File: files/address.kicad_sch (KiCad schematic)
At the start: 2 parts, among them J1 VLB_slot

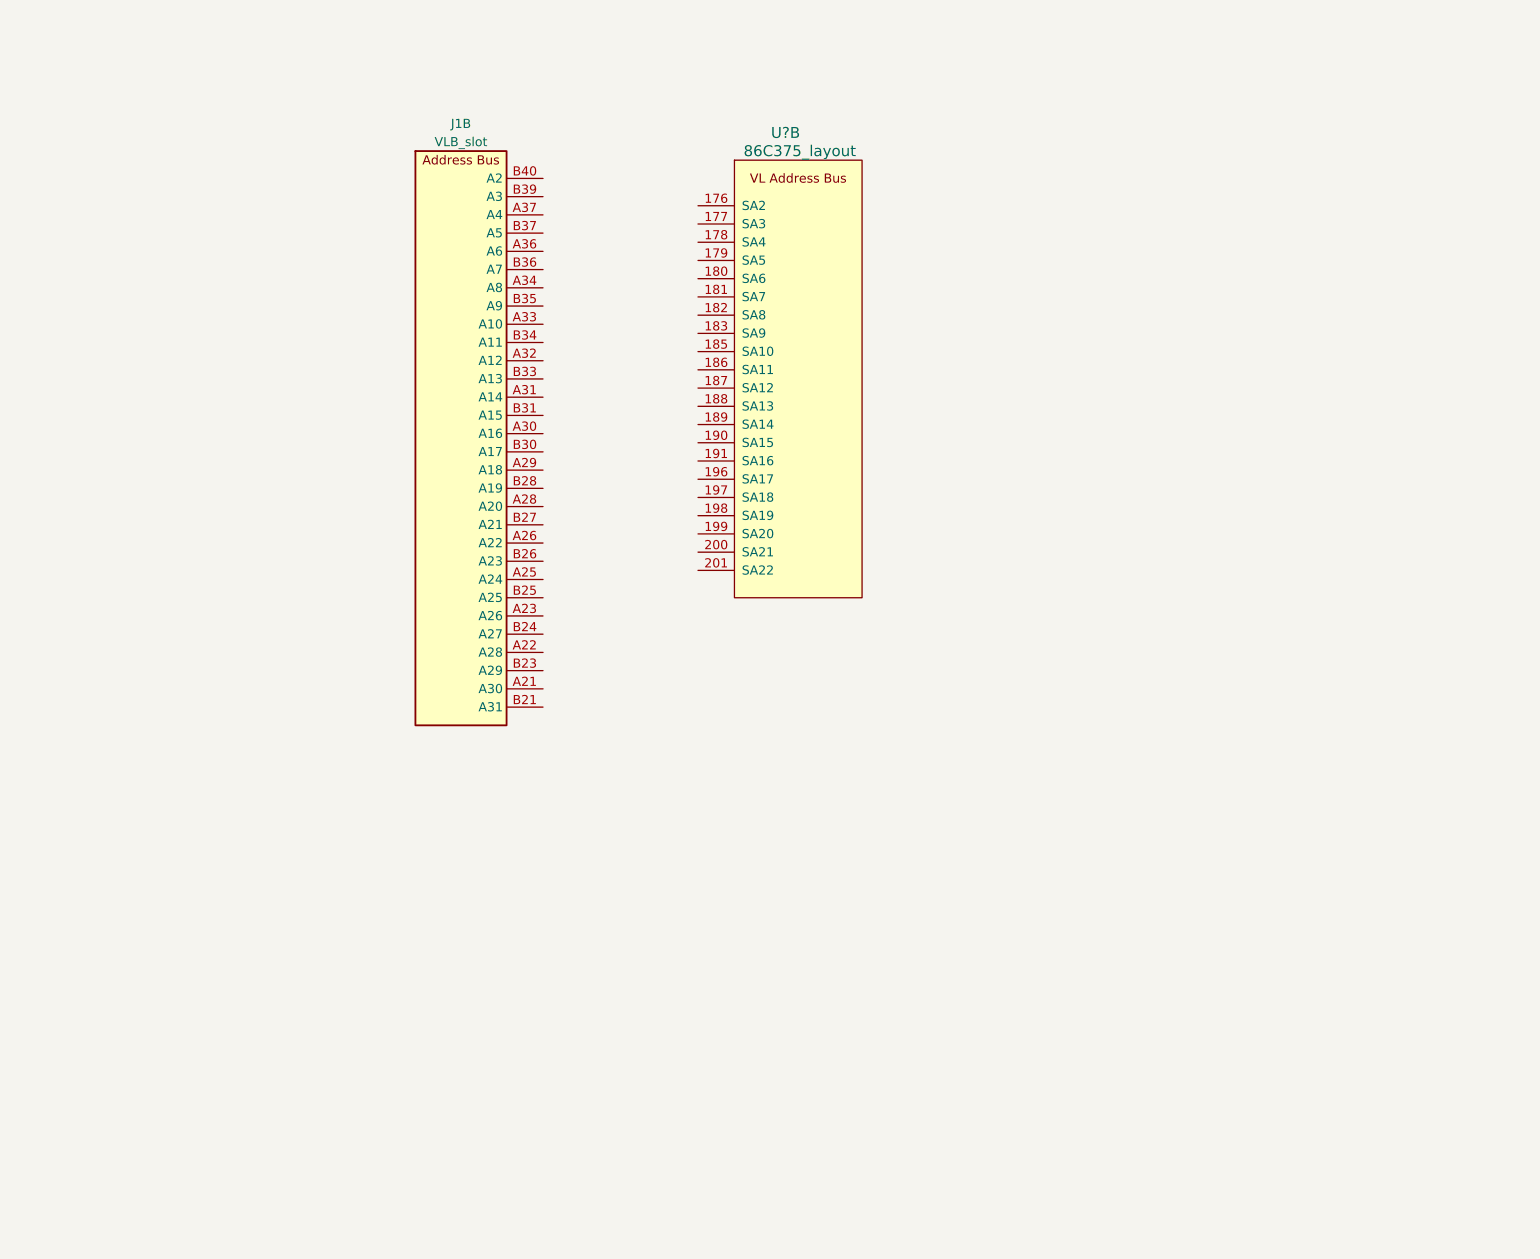
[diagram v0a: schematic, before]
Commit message: work on the memory bus, fixed symbols
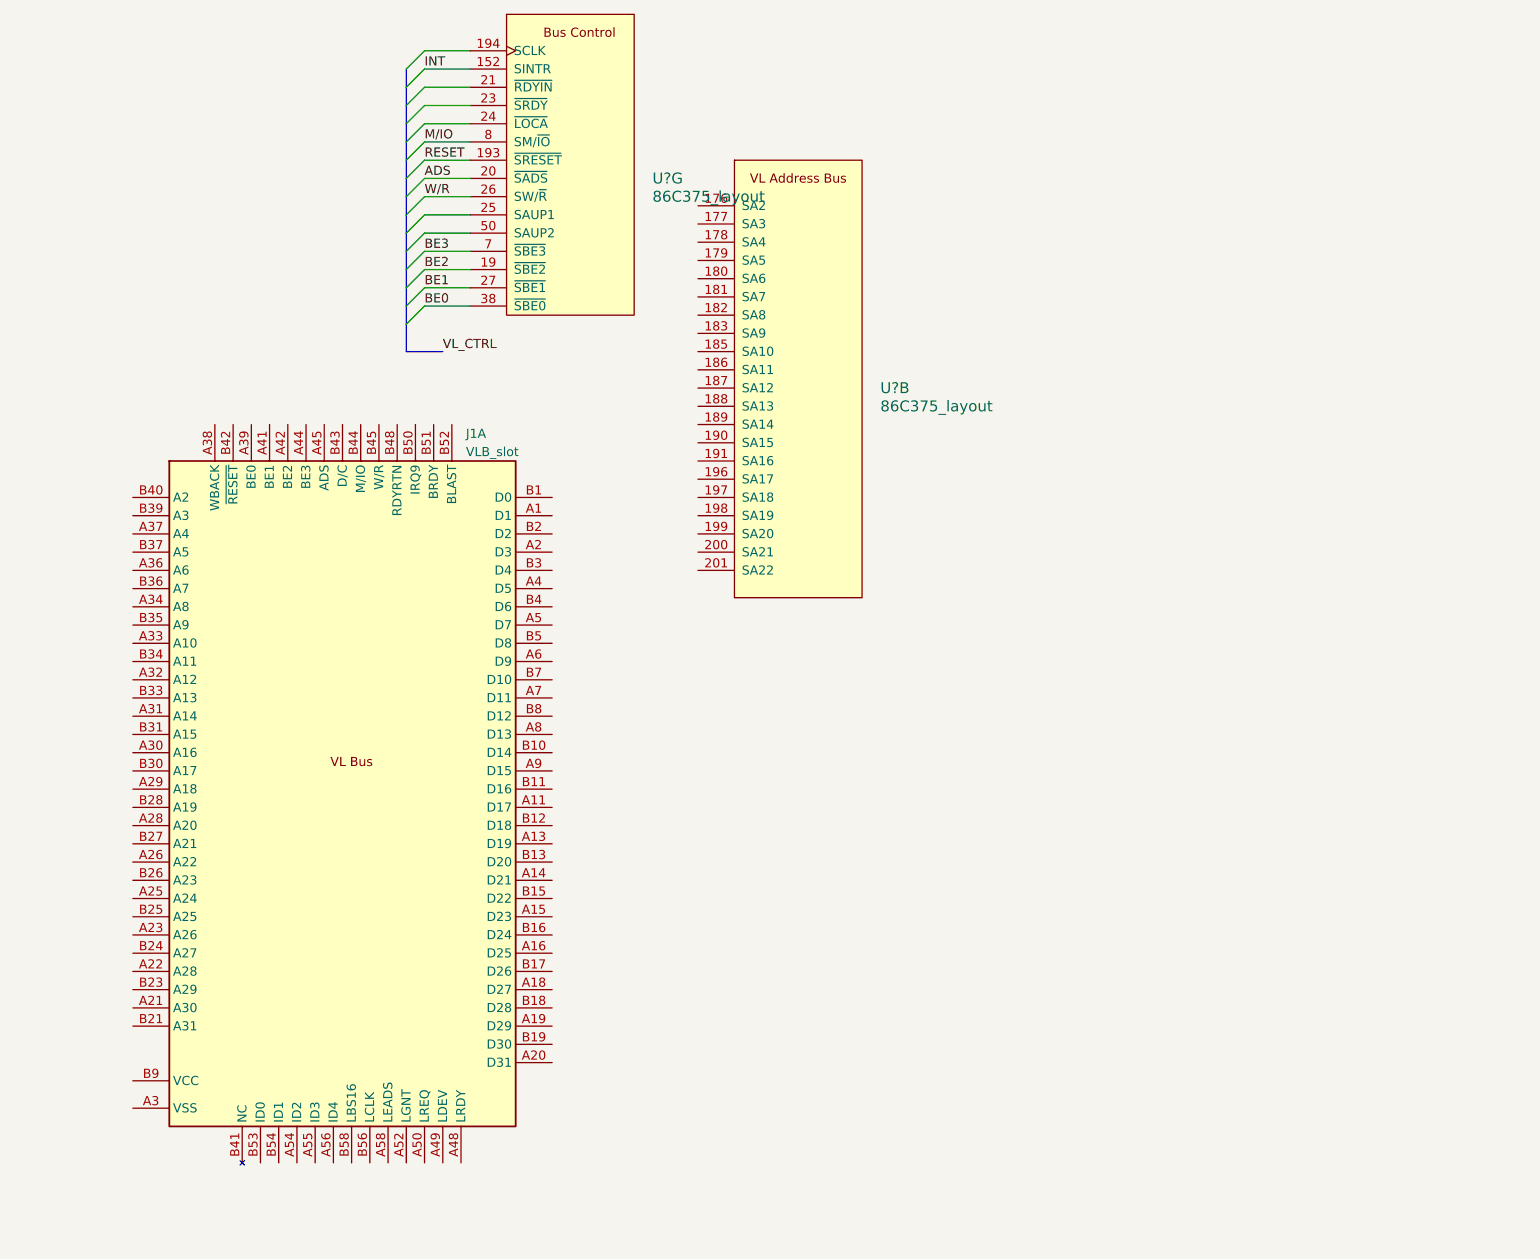
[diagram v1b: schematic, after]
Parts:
- removed J1: VLB_slot, symbol virge:VLB_slot
- added J1: VLB_slot, VLB:BUS_VLB_Board, symbol virge:VLB_slot
- added U?: 86C375_layout, Package_QFP:PQFP-208_28x28mm_P0.5mm, symbol virge:86C375_layout
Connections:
- new net: J1.A10 (VSS), J1.A17 (VSS), J1.A24 (VSS), J1.A3 (VSS), J1.A35 (VSS), J1.A43 (VSS), J1.A51 (VSS), J1.B14 (VSS), J1.B22 (VSS), J1.B29 (VSS), J1.B38 (VSS), J1.B49 (VSS), J1.B55 (VSS), J1.B6 (VSS)
- new net: J1.A12 (VCC), J1.A27 (VCC), J1.A40 (VCC), J1.A53 (VCC), J1.B20 (VCC), J1.B32 (VCC), J1.B57 (VCC), J1.B9 (VCC)
- new net: J1.A57 (NC), J1.B41 (NC)
- new net ADS: U?.20 (~{SADS})
- new net BE0: U?.38 (~{SBE0})
- new net BE1: U?.27 (~{SBE1})
- new net BE2: U?.19 (~{SBE2})
- new net BE3: U?.7 (~{SBE3})
- new net INT: U?.152 (SINTR)
- new net M/IO: U?.8 (SM/~{IO})
- new net RESET: U?.193 (~{SRESET})
- new net W/R: U?.26 (SW/~{R})

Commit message: changed memory chips, more progress
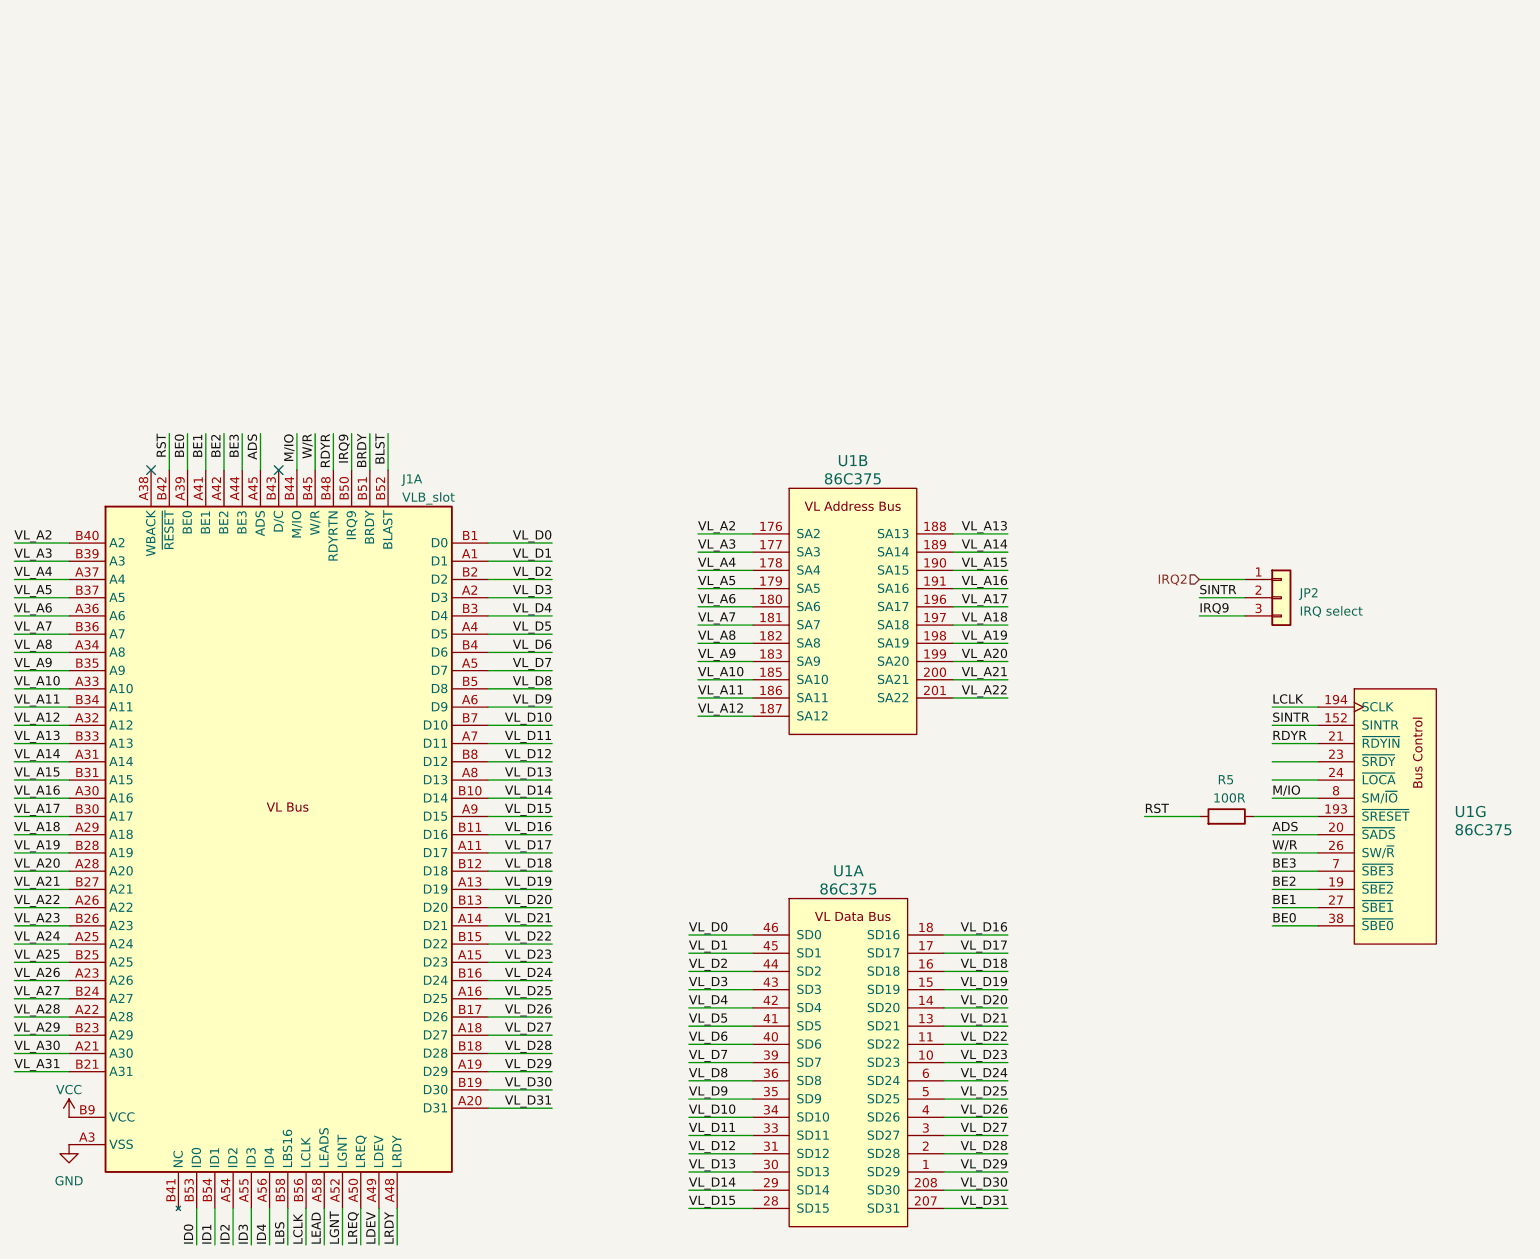
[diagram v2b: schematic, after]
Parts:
- removed U? (x2): 86C375_layout, Package_QFP:PQFP-208_28x28mm_P0.5mm, symbol virge:86C375_layout
- added JP2: IRQ select, Connector_PinHeader_2.54mm:PinHeader_1x03_P2.54mm_Vertical, symbol Connector_Generic:Conn_01x03
- added R5: 100R, Resistor_SMD:R_0805_2012Metric_Pad1.20x1.40mm_HandSolder, symbol Device:R
- added U1: 86C375, Package_QFP:PQFP-208_28x28mm_P0.5mm, symbol virge:86C375
- J1: footprint VLB:BUS_VLB_Board -> (none)
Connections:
- net ADS: now also J1.A45 (ADS), U1.20 (~{SADS})
- net BE0: now also J1.A39 (BE0), U1.38 (~{SBE0})
- net BE1: now also J1.A41 (BE1), U1.27 (~{SBE1})
- net BE2: now also J1.A42 (BE2), U1.19 (~{SBE2})
- net BE3: now also J1.A44 (BE3), U1.7 (~{SBE3})
- net M/IO: now also J1.B44 (M/IO), U1.8 (SM/~{IO})
- net W/R: now also J1.B45 (W/R), U1.26 (SW/~{R})
- net VL_D1: now reaches J1.A1 (D1)
- net VL_D1: now also U1.45 (SD1)
- net GND: now reaches J1.A10 (VSS), J1.A17 (VSS), J1.A24 (VSS), J1.A3 (VSS), J1.A35 (VSS), J1.A43 (VSS), J1.A51 (VSS), J1.B14 (VSS), J1.B22 (VSS), J1.B29 (VSS), J1.B38 (VSS), J1.B49 (VSS), J1.B55 (VSS), J1.B6 (VSS)
- net VL_D17: now reaches J1.A11 (D17)
- net VL_D17: now also U1.17 (SD17)
- net VCC: now reaches J1.A12 (VCC), J1.A27 (VCC), J1.A40 (VCC), J1.A53 (VCC), J1.B20 (VCC), J1.B32 (VCC), J1.B57 (VCC), J1.B9 (VCC)
- net VL_D19: now reaches J1.A13 (D19)
- net VL_D19: now also U1.15 (SD19)
- net VL_D21: now reaches J1.A14 (D21)
- net VL_D21: now also U1.13 (SD21)
- net VL_D23: now reaches J1.A15 (D23)
- net VL_D23: now also U1.10 (SD23)
- net VL_D25: now reaches J1.A16 (D25)
- net VL_D25: now also U1.5 (SD25)
- net VL_D27: now reaches J1.A18 (D27)
- net VL_D27: now also U1.3 (SD27)
- net VL_D29: now reaches J1.A19 (D29)
- net VL_D29: now also U1.1 (SD29)
- net VL_D3: now reaches J1.A2 (D3)
- net VL_D3: now also U1.43 (SD3)
- net VL_D31: now reaches J1.A20 (D31)
- net VL_D31: now also U1.207 (SD31)
- net VL_A30: now reaches J1.A21 (A30)
- net VL_A28: now reaches J1.A22 (A28)
- net VL_A26: now reaches J1.A23 (A26)
- net VL_A24: now reaches J1.A25 (A24)
- net VL_A22: now reaches J1.A26 (A22)
- net VL_A22: now also U1.201 (SA22)
- net VL_A20: now reaches J1.A28 (A20)
- net VL_A20: now also U1.199 (SA20)
- net VL_A18: now reaches J1.A29 (A18)
- net VL_A18: now also U1.197 (SA18)
- net VL_A16: now reaches J1.A30 (A16)
- net VL_A16: now also U1.191 (SA16)
- net VL_A14: now reaches J1.A31 (A14)
- net VL_A14: now also U1.189 (SA14)
- net VL_A12: now reaches J1.A32 (A12)
- net VL_A12: now also U1.187 (SA12)
- net VL_A10: now reaches J1.A33 (A10)
- net VL_A10: now also U1.185 (SA10)
- net VL_A8: now reaches J1.A34 (A8)
- net VL_A8: now also U1.182 (SA8)
- net VL_A6: now reaches J1.A36 (A6)
- net VL_A6: now also U1.180 (SA6)
- net VL_A4: now reaches J1.A37 (A4)
- net VL_A4: now also U1.178 (SA4)
- net VL_D5: now reaches J1.A4 (D5)
- net VL_D5: now also U1.41 (SD5)
- net LRDY: now reaches J1.A48 (LRDY)
- net LDEV: now reaches J1.A49 (LDEV)
- net VL_D7: now reaches J1.A5 (D7)
- net VL_D7: now also U1.39 (SD7)
- net LREQ: now reaches J1.A50 (LREQ)
- net LGNT: now reaches J1.A52 (LGNT)
- net ID2: now reaches J1.A54 (ID2)
- net ID3: now reaches J1.A55 (ID3)
- net ID4: now reaches J1.A56 (ID4)
- net LEAD: now reaches J1.A58 (LEADS)
- net VL_D9: now reaches J1.A6 (D9)
- net VL_D9: now also U1.35 (SD9)
- net VL_D11: now reaches J1.A7 (D11)
- net VL_D11: now also U1.33 (SD11)
- net VL_D13: now reaches J1.A8 (D13)
- net VL_D13: now also U1.30 (SD13)
- net VL_D15: now reaches J1.A9 (D15)
- net VL_D15: now also U1.28 (SD15)
- net VL_D0: now reaches J1.B1 (D0)
- net VL_D0: now also U1.46 (SD0)
- net VL_D14: now reaches J1.B10 (D14)
- net VL_D14: now also U1.29 (SD14)
- net VL_D16: now reaches J1.B11 (D16)
- net VL_D16: now also U1.18 (SD16)
- net VL_D18: now reaches J1.B12 (D18)
- net VL_D18: now also U1.16 (SD18)
- net VL_D20: now reaches J1.B13 (D20)
- net VL_D20: now also U1.14 (SD20)
- net VL_D22: now reaches J1.B15 (D22)
- net VL_D22: now also U1.11 (SD22)
- net VL_D24: now reaches J1.B16 (D24)
- net VL_D24: now also U1.6 (SD24)
- net VL_D26: now reaches J1.B17 (D26)
- net VL_D26: now also U1.4 (SD26)
- net VL_D28: now reaches J1.B18 (D28)
- net VL_D28: now also U1.2 (SD28)
- net VL_D30: now reaches J1.B19 (D30)
- net VL_D30: now also U1.208 (SD30)
- net VL_D2: now reaches J1.B2 (D2)
- net VL_D2: now also U1.44 (SD2)
- net VL_A31: now reaches J1.B21 (A31)
- net VL_A29: now reaches J1.B23 (A29)
- net VL_A27: now reaches J1.B24 (A27)
- net VL_A25: now reaches J1.B25 (A25)
- net VL_A23: now reaches J1.B26 (A23)
- net VL_A21: now reaches J1.B27 (A21)
- net VL_A21: now also U1.200 (SA21)
- net VL_A19: now reaches J1.B28 (A19)
- net VL_A19: now also U1.198 (SA19)
- net VL_D4: now reaches J1.B3 (D4)
- net VL_D4: now also U1.42 (SD4)
- net VL_A17: now reaches J1.B30 (A17)
- net VL_A17: now also U1.196 (SA17)
- net VL_A15: now reaches J1.B31 (A15)
- net VL_A15: now also U1.190 (SA15)
- net VL_A13: now reaches J1.B33 (A13)
- net VL_A13: now also U1.188 (SA13)
- net VL_A11: now reaches J1.B34 (A11)
- net VL_A11: now also U1.186 (SA11)
- net VL_A9: now reaches J1.B35 (A9)
- net VL_A9: now also U1.183 (SA9)
- net VL_A7: now reaches J1.B36 (A7)
- net VL_A7: now also U1.181 (SA7)
- net VL_A5: now reaches J1.B37 (A5)
- net VL_A5: now also U1.179 (SA5)
- net VL_A3: now reaches J1.B39 (A3)
- net VL_A3: now also U1.177 (SA3)
- net VL_D6: now reaches J1.B4 (D6)
- net VL_D6: now also U1.40 (SD6)
- net VL_A2: now reaches J1.B40 (A2)
- net VL_A2: now also U1.176 (SA2)
- net RST: now reaches J1.B42 (~{RESET})
- net RST: now also R5.2
- net RDYR: now reaches J1.B48 (RDYRTN)
- net RDYR: now also U1.21 (~{RDYIN})
- net VL_D8: now reaches J1.B5 (D8)
- net VL_D8: now also U1.36 (SD8)
- net IRQ9: now reaches J1.B50 (IRQ9)
- net IRQ9: now also JP2.3 (Pin_3)
- net BRDY: now reaches J1.B51 (BRDY)
- net BLST: now reaches J1.B52 (BLAST)
- net ID0: now reaches J1.B53 (ID0)
- net ID1: now reaches J1.B54 (ID1)
- net LCLK: now reaches J1.B56 (LCLK)
- net LCLK: now also U1.194 (SCLK)
- net LBS: now reaches J1.B58 (LBS16)
- net VL_D10: now reaches J1.B7 (D10)
- net VL_D10: now also U1.34 (SD10)
- net VL_D12: now reaches J1.B8 (D12)
- net VL_D12: now also U1.31 (SD12)
- new net: R5.1, U1.193 (~{SRESET})
- new net IRQ2: JP2.1 (Pin_1)
- new net SINTR: JP2.2 (Pin_2), U1.152 (SINTR)
- no-connect marks 0 -> 2
